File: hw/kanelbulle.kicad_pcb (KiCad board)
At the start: 2 copper layers, 48.8 x 48.8 mm, 54 parts, among them J1 USB, U1 LPC1114/302, U2 PCA9685

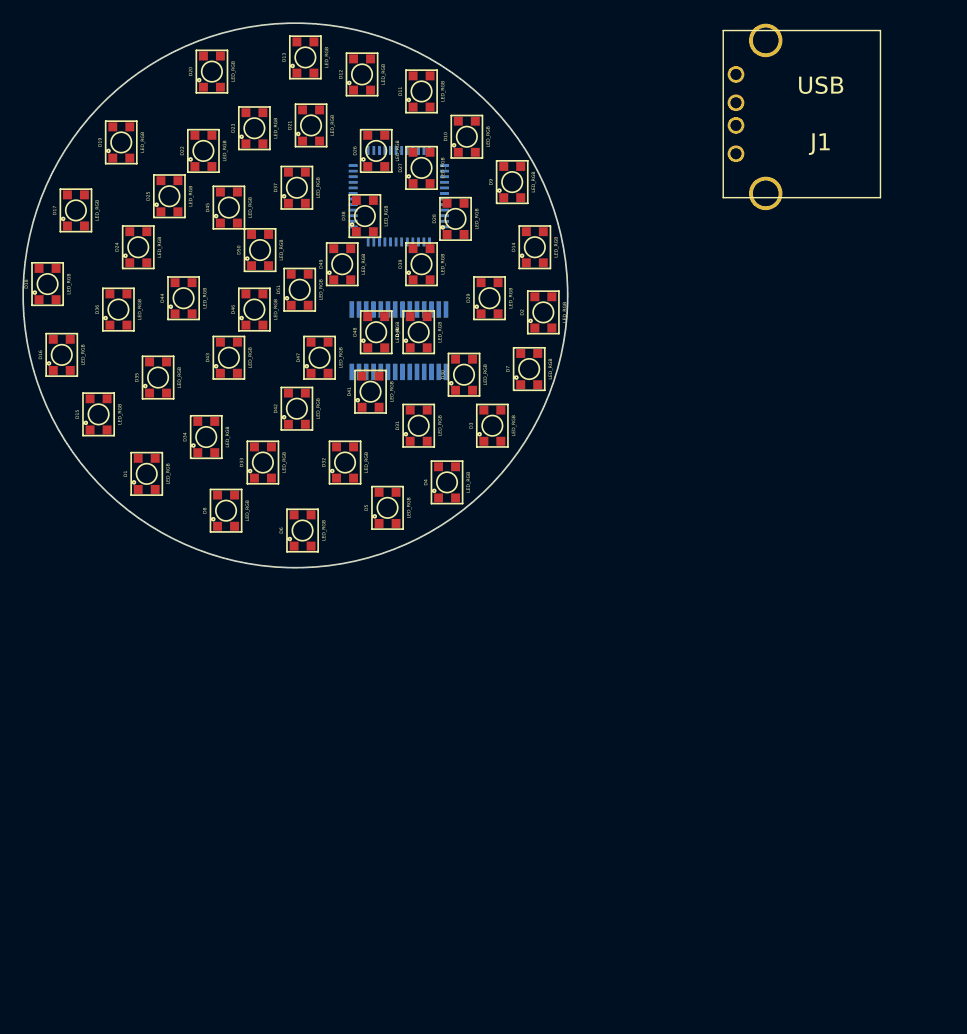
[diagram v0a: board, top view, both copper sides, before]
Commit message: Moved all LEDs
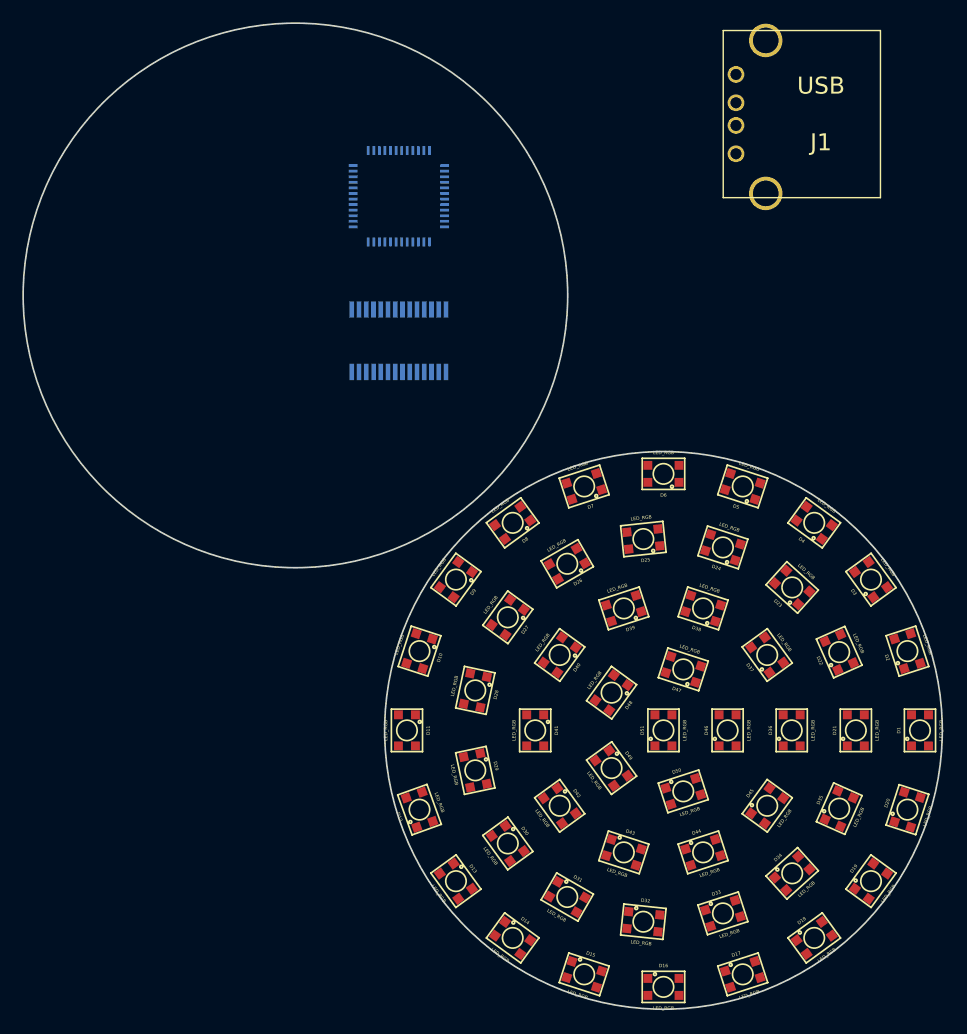
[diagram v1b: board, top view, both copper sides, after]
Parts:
- moved D19 94.4 mm to (218.6, 163.5), turned to 324 degrees
- moved D20 90.9 mm to (221.9, 157.1), turned to 342 degrees
- moved D17 90.9 mm to (207.1, 171.9), turned to 288 degrees
- moved D18 90.3 mm to (213.5, 168.6), turned to 306 degrees
- moved D16 78.2 mm to (200.0, 173.0), turned to 270 degrees
- moved D13 75.1 mm to (181.4, 163.5), turned to 216 degrees
- moved D1 73.0 mm to (223.0, 150.0)
- moved D21 73.0 mm to (217.2, 150.0)
- moved D22 72.6 mm to (215.8, 143.0), turned to 24 degrees
- moved D35 72.3 mm to (215.8, 157.0), turned to 336 degrees
- moved D45 72.2 mm to (209.3, 156.8), turned to 324 degrees
- moved D36 71.2 mm to (211.5, 150.0)
- moved D44 68.1 mm to (203.6, 160.9), turned to 288 degrees
- moved D15 66.5 mm to (192.9, 171.9), turned to 252 degrees
- moved D12 66.1 mm to (178.1, 157.1), turned to 19.8 degrees
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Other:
- board size 48.8 x 48.8 mm -> 82.4 x 88.4 mm

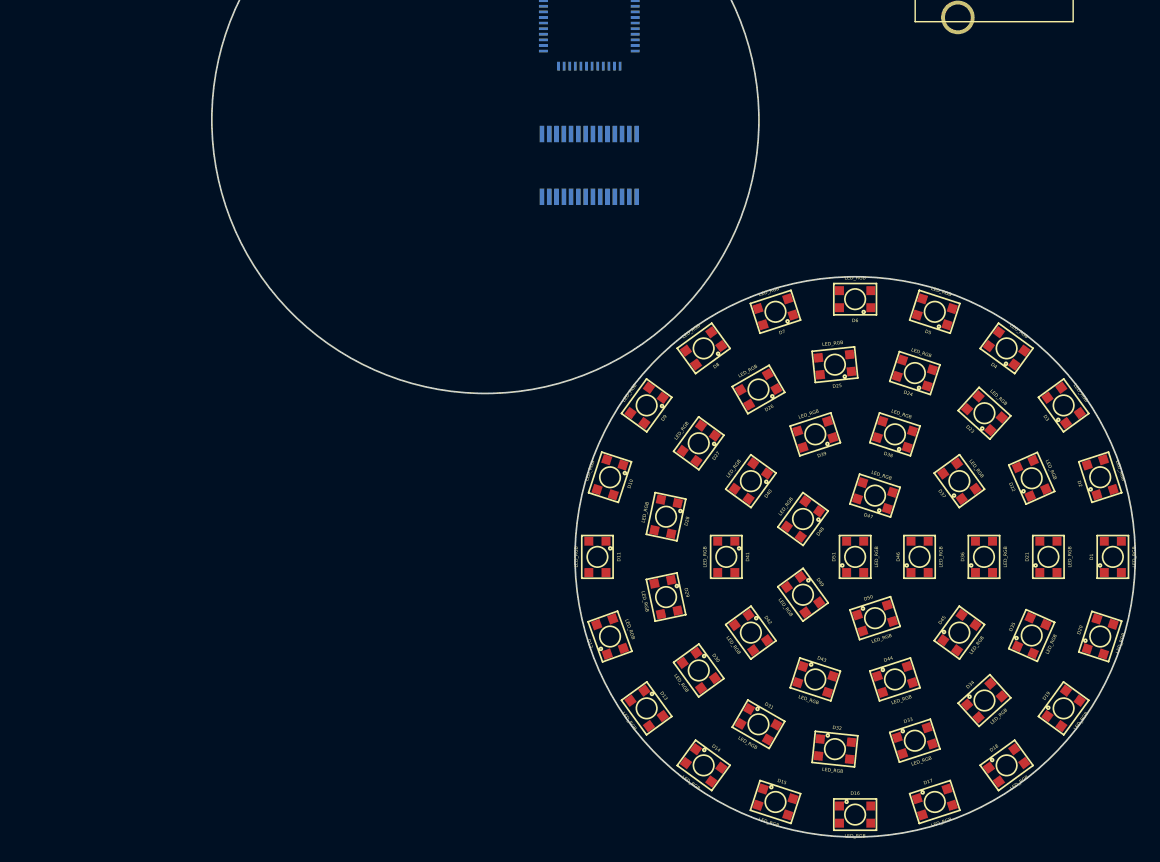
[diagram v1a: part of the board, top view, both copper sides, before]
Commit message: connected leds on schematic
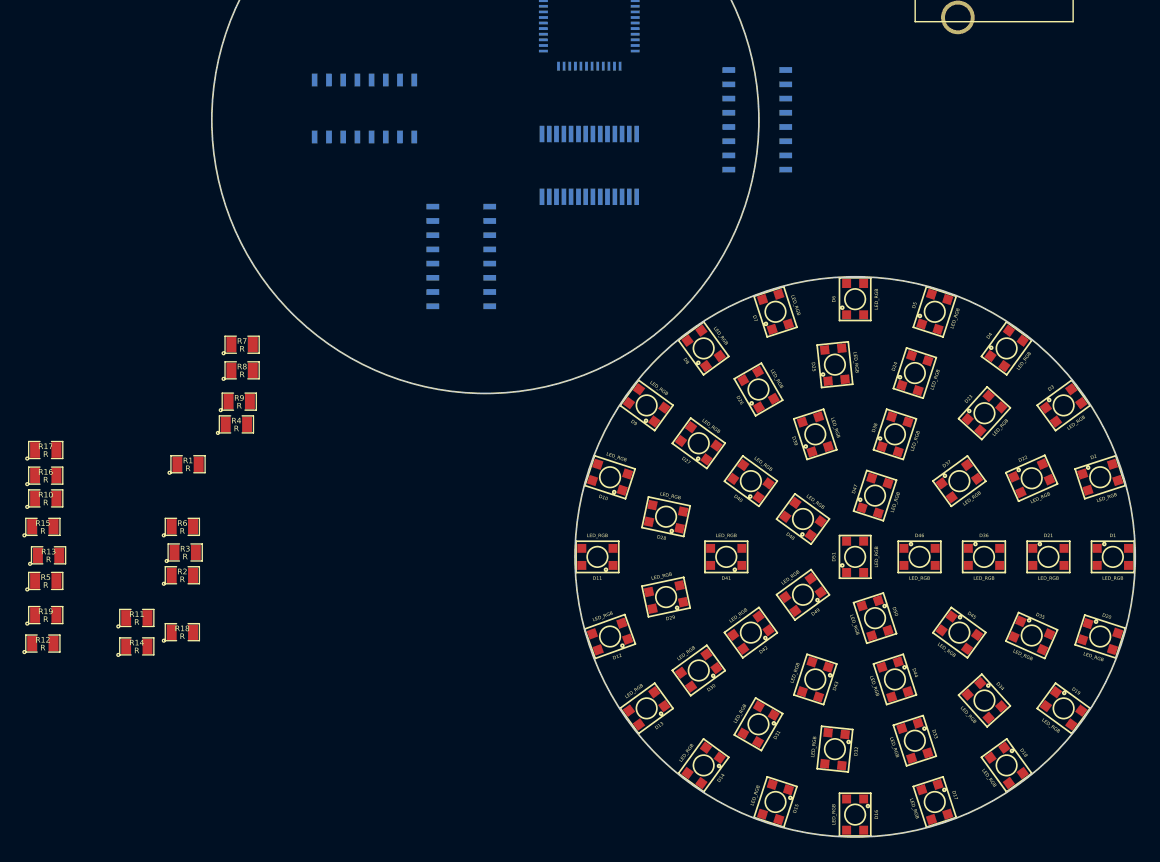
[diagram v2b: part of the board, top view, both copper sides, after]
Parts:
- added R1: R, SM0805, F.Cu at (140.5, 141.7)
- added R10: R, SM0805, F.Cu at (127.8, 144.8)
- added R11: R, SM0805, F.Cu at (135.9, 155.4)
- added R12: R, SM0805, F.Cu at (127.5, 157.7)
- added R13: R, SM0805, F.Cu at (128.0, 149.9)
- added R14: R, SM0805, F.Cu at (135.9, 158.0)
- added R15: R, SM0805, F.Cu at (127.5, 147.3)
- added R16: R, SM0805, F.Cu at (127.8, 142.7)
- added R17: R, SM0805, F.Cu at (127.8, 140.5)
- added R18: R, SM0805, F.Cu at (140.0, 156.7)
- added R19: R, SM0805, F.Cu at (127.8, 155.2)
- added R2: R, SM0805, F.Cu at (140.0, 151.6)
- added R3: R, SM0805, F.Cu at (140.2, 149.6)
- added R4: R, SM0805, F.Cu at (144.8, 138.2)
- added R5: R, SM0805, F.Cu at (127.8, 152.1)
- added R6: R, SM0805, F.Cu at (140.0, 147.3)
- added R7: R, SM0805, F.Cu at (145.3, 131.1)
- added R8: R, SM0805, F.Cu at (145.3, 133.3)
- added R9: R, SM0805, F.Cu at (145.0, 136.1)
- added U3: ULN2003A, SO16E, B.Cu at (156.2, 110.0)
- added U4: ULN2003A, SO16E, B.Cu at (191.3, 111.0)
- added U5: ULN2003A, SO16E, B.Cu at (164.8, 123.2)
- turned D1 to 270 degrees
- turned D10 to 72 degrees
- turned D11 to 90 degrees
- turned D12 to 109.8 degrees
- turned D13 to 126 degrees
- turned D14 to 144 degrees
- turned D15 to 162 degrees
- turned D16 to 180 degrees
- turned D17 to 198 degrees
- turned D18 to 216 degrees
- turned D19 to 234 degrees
- turned D2 to 288 degrees
- turned D20 to 252 degrees
- turned D21 to 270 degrees
- turned D22 to 294 degrees
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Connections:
- D1 pad 1: (no net) -> 3V3
- D1 pad 2: (no net) -> /R1
- D1 pad 3: (no net) -> /G1
- D1 pad 4: (no net) -> /B1
- D10 pad 1: (no net) -> 3V3
- D10 pad 2: (no net) -> /R1
- D10 pad 3: (no net) -> /G1
- D10 pad 4: (no net) -> /B1
- D11 pad 1: (no net) -> 3V3
- D11 pad 2: (no net) -> /R1
- D11 pad 3: (no net) -> /G1
- D11 pad 4: (no net) -> /B1
- D12 pad 1: (no net) -> 3V3
- D12 pad 2: (no net) -> /R1
- D12 pad 3: (no net) -> /G1
- D12 pad 4: (no net) -> /B1
- D13 pad 1: (no net) -> 3V3
- D13 pad 2: (no net) -> /R1
- D13 pad 3: (no net) -> /G1
- D13 pad 4: (no net) -> /B1
- D14 pad 1: (no net) -> 3V3
- D14 pad 2: (no net) -> /R1
- D14 pad 3: (no net) -> /G1
- D14 pad 4: (no net) -> /B1
- D15 pad 1: (no net) -> 3V3
- D15 pad 2: (no net) -> /R1
- D15 pad 3: (no net) -> /G1
- D15 pad 4: (no net) -> /B1
- D16 pad 1: (no net) -> 3V3
- D16 pad 2: (no net) -> /R1
- D16 pad 3: (no net) -> /G1
- D16 pad 4: (no net) -> /B1
- D17 pad 1: (no net) -> 3V3
- D17 pad 2: (no net) -> /R1
- D17 pad 3: (no net) -> /G1
- D17 pad 4: (no net) -> /B1
- D18 pad 1: (no net) -> 3V3
- D18 pad 2: (no net) -> /R1
- D18 pad 3: (no net) -> /G1
- D18 pad 4: (no net) -> /B1
- D19 pad 1: (no net) -> 3V3
- D19 pad 2: (no net) -> /R1
- D19 pad 3: (no net) -> /G1
- D19 pad 4: (no net) -> /B1
- D2 pad 1: (no net) -> 3V3
- D2 pad 2: (no net) -> /R1
- D2 pad 3: (no net) -> /G1
- D2 pad 4: (no net) -> /B1
- D20 pad 1: (no net) -> 3V3
- D21 pad 1: (no net) -> 3V3
- D21 pad 2: (no net) -> /R2
- D21 pad 3: (no net) -> /G2
- D21 pad 4: (no net) -> /B2
- D22 pad 1: (no net) -> 3V3
- D22 pad 2: (no net) -> /R2
- D22 pad 3: (no net) -> /G2
- D22 pad 4: (no net) -> /B2
- D23 pad 1: (no net) -> 3V3
- D23 pad 2: (no net) -> /R2
- D23 pad 3: (no net) -> /G2
- D23 pad 4: (no net) -> /B2
- D24 pad 1: (no net) -> 3V3
- D24 pad 2: (no net) -> /R2
- D24 pad 3: (no net) -> /G2
- D24 pad 4: (no net) -> /B2
- D25 pad 1: (no net) -> 3V3
- D25 pad 2: (no net) -> /R2
- D25 pad 3: (no net) -> /G2
- D25 pad 4: (no net) -> /B2
- D26 pad 1: (no net) -> 3V3
- D26 pad 2: (no net) -> /R2
- D26 pad 3: (no net) -> /G2
- D26 pad 4: (no net) -> /B2
- D27 pad 1: (no net) -> 3V3
- D27 pad 2: (no net) -> /R2
- D27 pad 3: (no net) -> /G2
- D27 pad 4: (no net) -> /B2
- D28 pad 1: (no net) -> 3V3
- D28 pad 2: (no net) -> /R2
- D28 pad 3: (no net) -> /G2
- D28 pad 4: (no net) -> /B2
- D29 pad 1: (no net) -> 3V3
- D29 pad 2: (no net) -> /R2
- D29 pad 3: (no net) -> /G2
- D29 pad 4: (no net) -> /B2
- D3 pad 1: (no net) -> 3V3
- D3 pad 2: (no net) -> /R1
- D3 pad 3: (no net) -> /G1
- D3 pad 4: (no net) -> /B1
- D30 pad 1: (no net) -> 3V3
- D30 pad 2: (no net) -> /R2
- D30 pad 3: (no net) -> /G2
- D30 pad 4: (no net) -> /B2
- D31 pad 1: (no net) -> 3V3
- D31 pad 2: (no net) -> /R2
- D31 pad 3: (no net) -> /G2
- D31 pad 4: (no net) -> /B2
- D32 pad 1: (no net) -> 3V3
- D32 pad 2: (no net) -> /R2
- D32 pad 3: (no net) -> /G2
- D32 pad 4: (no net) -> /B2
- D33 pad 1: (no net) -> 3V3
- D33 pad 2: (no net) -> /R2
- D33 pad 3: (no net) -> /G2
- D33 pad 4: (no net) -> /B2
- D34 pad 1: (no net) -> 3V3
- D34 pad 2: (no net) -> /R2
- D34 pad 3: (no net) -> /G2
- D34 pad 4: (no net) -> /B2
- D35 pad 1: (no net) -> 3V3
- D35 pad 2: (no net) -> /R2
- D35 pad 3: (no net) -> /G2
- D35 pad 4: (no net) -> /B2
- D36 pad 1: (no net) -> 3V3
- D36 pad 2: (no net) -> /R3
- D36 pad 3: (no net) -> /G3
- D36 pad 4: (no net) -> /B3
- D37 pad 1: (no net) -> 3V3
- D37 pad 2: (no net) -> /R3
- D37 pad 3: (no net) -> /G3
- D37 pad 4: (no net) -> /B3
- D38 pad 1: (no net) -> 3V3
- D38 pad 2: (no net) -> /R3
- D38 pad 3: (no net) -> /G3
- D38 pad 4: (no net) -> /B3
- D39 pad 1: (no net) -> 3V3
- D39 pad 2: (no net) -> /R3
- D39 pad 3: (no net) -> /G3
- D39 pad 4: (no net) -> /B3
- D4 pad 1: (no net) -> 3V3
- D4 pad 2: (no net) -> /R1
- D4 pad 3: (no net) -> /G1
- D4 pad 4: (no net) -> /B1
- D40 pad 1: (no net) -> 3V3
- D40 pad 2: (no net) -> /R3
- D40 pad 3: (no net) -> /G3
- D40 pad 4: (no net) -> /B3
- D41 pad 1: (no net) -> 3V3
- D41 pad 2: (no net) -> /R3
- D41 pad 3: (no net) -> /G3
- D41 pad 4: (no net) -> /B3
- D42 pad 1: (no net) -> 3V3
- D42 pad 2: (no net) -> /R3
- D42 pad 3: (no net) -> /G3
- D42 pad 4: (no net) -> /B3
- D43 pad 1: (no net) -> 3V3
- D43 pad 2: (no net) -> /R3
- D43 pad 3: (no net) -> /G3
- D43 pad 4: (no net) -> /B3
- D44 pad 1: (no net) -> 3V3
- D44 pad 2: (no net) -> /R3
- D44 pad 3: (no net) -> /G3
- D44 pad 4: (no net) -> /B3
- D45 pad 1: (no net) -> 3V3
- D45 pad 2: (no net) -> /R3
- D45 pad 3: (no net) -> /G3
- D45 pad 4: (no net) -> /B3
- D46 pad 1: (no net) -> 3V3
- D46 pad 2: (no net) -> /R4
- D46 pad 3: (no net) -> /G4
- D46 pad 4: (no net) -> /B4
- D47 pad 1: (no net) -> 3V3
- D47 pad 2: (no net) -> /R4
- D47 pad 3: (no net) -> /G4
- D47 pad 4: (no net) -> /B4
- D48 pad 1: (no net) -> 3V3
- D48 pad 2: (no net) -> /R4
- D48 pad 3: (no net) -> /G4
- D48 pad 4: (no net) -> /B4
- D49 pad 1: (no net) -> 3V3
- D49 pad 2: (no net) -> /R4
- D49 pad 3: (no net) -> /G4
- D49 pad 4: (no net) -> /B4
- D5 pad 1: (no net) -> 3V3
- D5 pad 2: (no net) -> /R1
- D5 pad 3: (no net) -> /G1
- D5 pad 4: (no net) -> /B1
- D50 pad 1: (no net) -> 3V3
- D50 pad 2: (no net) -> /R4
- D50 pad 3: (no net) -> /G4
- D50 pad 4: (no net) -> /B4
- D51 pad 1: (no net) -> 3V3
- D51 pad 2: (no net) -> /R5
- D51 pad 3: (no net) -> /G5
- D51 pad 4: (no net) -> /B5
- D6 pad 1: (no net) -> 3V3
- D6 pad 2: (no net) -> /R1
- D6 pad 3: (no net) -> /G1
- D6 pad 4: (no net) -> /B1
- D7 pad 1: (no net) -> 3V3
- D7 pad 2: (no net) -> /R1
- D7 pad 3: (no net) -> /G1
- D7 pad 4: (no net) -> /B1
- D8 pad 1: (no net) -> 3V3
- D8 pad 2: (no net) -> /R1
- D8 pad 3: (no net) -> /G1
- D8 pad 4: (no net) -> /B1
- D9 pad 1: (no net) -> 3V3
- D9 pad 2: (no net) -> /R1
- D9 pad 3: (no net) -> /G1
- D9 pad 4: (no net) -> /B1
- U1 pad 3: (no net) -> N-000006
- U1 pad 4: (no net) -> N-000007
- U1 pad 41: (no net) -> N-0000030
- U1 pad 44: (no net) -> 3V3
- U1 pad 5: (no net) -> N-0000030
- U1 pad 8: (no net) -> 3V3
- U2 pad 10: (no net) -> N-0000044
- U2 pad 11: (no net) -> N-0000042
- U2 pad 12: (no net) -> N-0000051
- U2 pad 13: (no net) -> N-0000052
- U2 pad 14: (no net) -> GND
- U2 pad 15: (no net) -> N-000009
- U2 pad 16: (no net) -> N-0000010
- U2 pad 17: (no net) -> N-0000011
- U2 pad 18: (no net) -> N-0000012
- U2 pad 19: (no net) -> N-0000013
- U2 pad 20: (no net) -> N-000008
- U2 pad 21: (no net) -> N-0000014
- U2 pad 25: (no net) -> GND
- U2 pad 26: (no net) -> /SCL
- U2 pad 27: (no net) -> /SDA
- U2 pad 28: (no net) -> 3V3
- U2 pad 6: (no net) -> N-0000060
- U2 pad 7: (no net) -> N-0000061
- U2 pad 8: (no net) -> N-000001
- U2 pad 9: (no net) -> N-0000043
